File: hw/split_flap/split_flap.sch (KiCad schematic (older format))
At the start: 22 parts, among them J1 Conn_01x02, J19 POWER, J2 Conn_01x02, J3 Conn_01x02, J4 Conn_01x02, J5 Conn_01x02, J6 Conn_01x02, J7 Conn_01x02, J8 Conn_01x02, SW1 SW_RESET, U1 PCF8574, U2 NodeMCU_1.0_(ESP-12E)

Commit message: hw: Supercharge PCB !
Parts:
- removed SW1: SW_RESET, Connector_PinHeader_2.54mm:PinHeader_1x02_P2.54mm_Vertical, symbol Switch:SW_Push
- added J17: Conn_01x05, Connector_JST:JST_XH_B5B-XH-A_1x05_P2.50mm_Vertical, symbol Connector_Generic:Conn_01x05
- added J23, J24, J25, J26: Conn_01x02, Connector_JST:JST_XH_B2B-XH-A_1x02_P2.50mm_Vertical, symbol Connector_Generic:Conn_01x02
- added R11, R12, R13, R14: R, Resistor_THT:R_Axial_DIN0207_L6.3mm_D2.5mm_P10.16mm_Horizontal, symbol Device:R
- added U15: PCF8574, Package_SO:SOIC-16W_7.5x10.3mm_P1.27mm, symbol Interface_Expansion:PCF8574
- U2: footprint ESP:NodeMCU1.0(12-E) -> ESP:ESP12F-Devkit-V3
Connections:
- wire segments 121 -> 175
- no-connect marks 22 -> 30
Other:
- moved on the sheet: J1, J19, J2, J3, J4, J5, J6, J7, J8, R1, R10, R2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

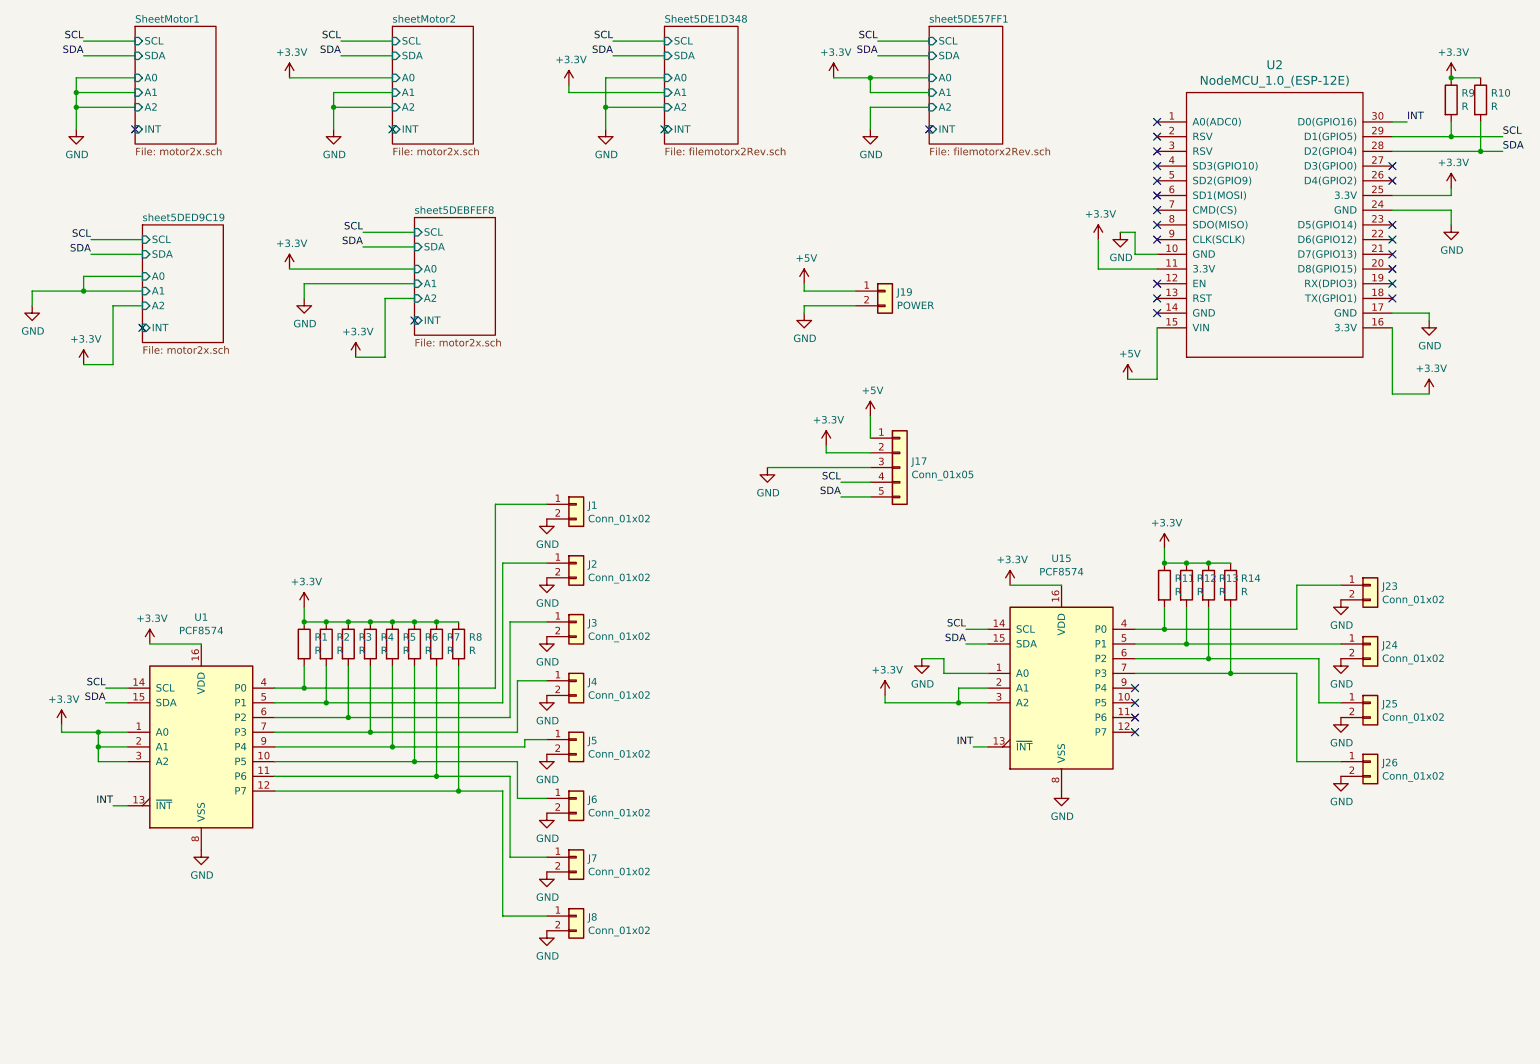
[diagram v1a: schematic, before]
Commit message: Reroute full PCB
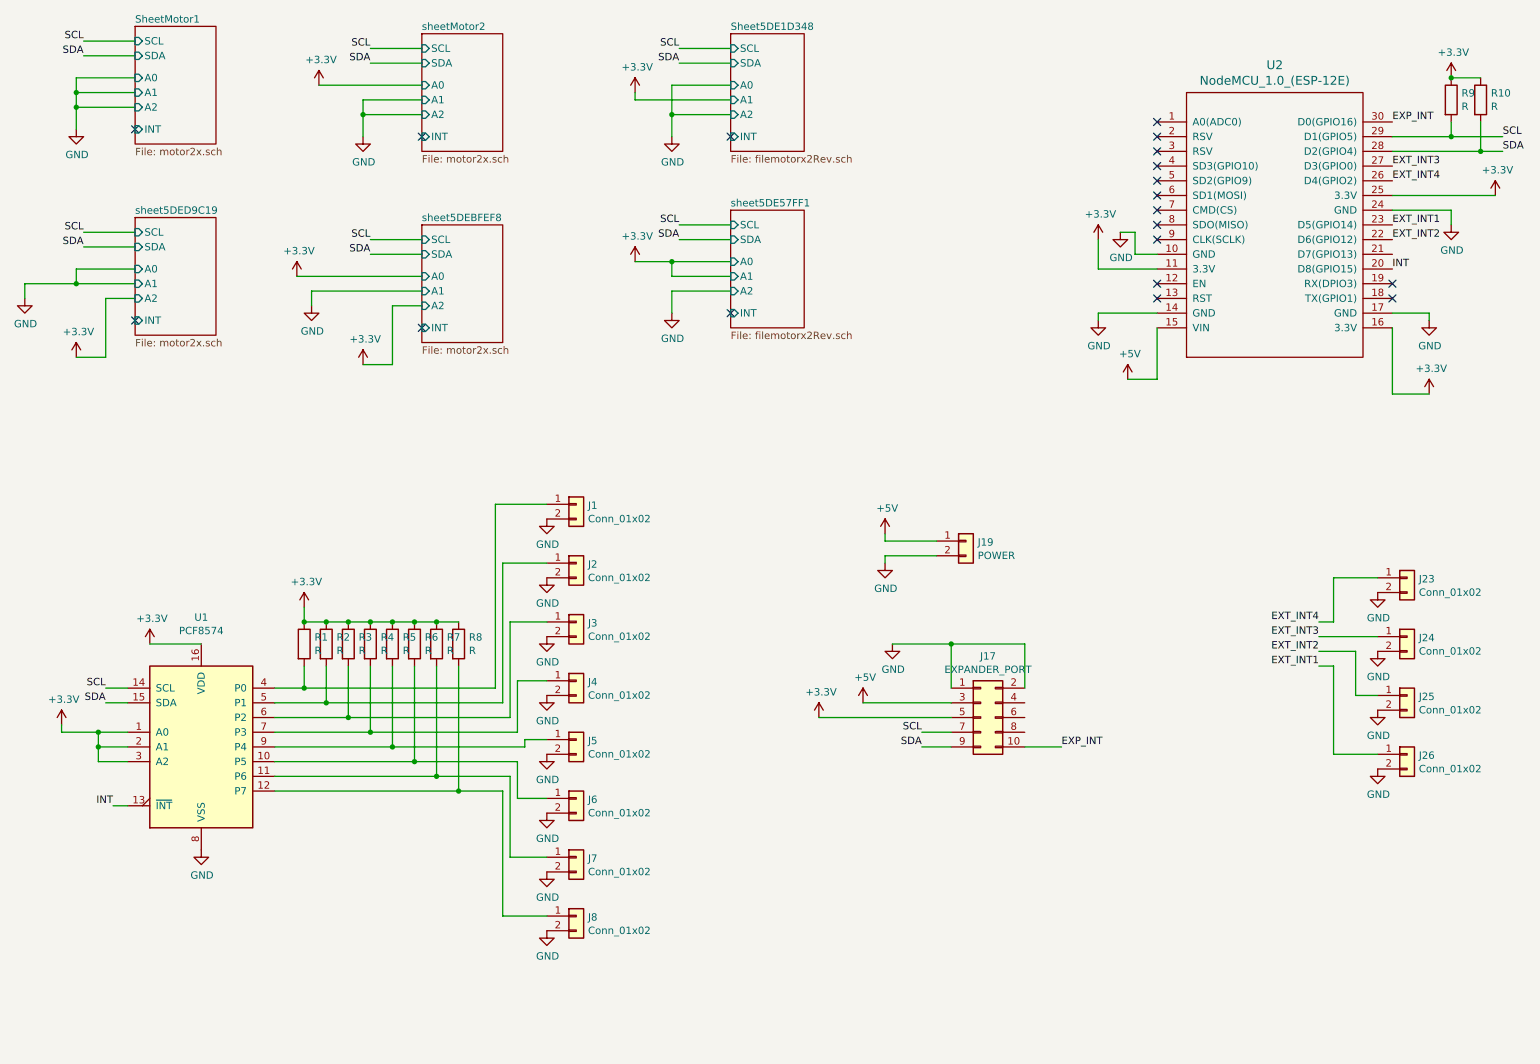
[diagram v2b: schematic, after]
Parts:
- removed J17: Conn_01x05, Connector_JST:JST_XH_B5B-XH-A_1x05_P2.50mm_Vertical, symbol Connector_Generic:Conn_01x05
- removed R11, R12, R13, R14: R, Resistor_THT:R_Axial_DIN0207_L6.3mm_D2.5mm_P10.16mm_Horizontal, symbol Device:R
- removed U15: PCF8574, Package_SO:SOIC-16W_7.5x10.3mm_P1.27mm, symbol Interface_Expansion:PCF8574
- added J17: EXPANDER_PORT, Connector_PinHeader_2.54mm:PinHeader_2x05_P2.54mm_Vertical, symbol Connector_Generic:Conn_02x05_Odd_Even
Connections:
- net +3V3: now also J17.5 (Pin_5)
- net +5V: now also J17.3 (Pin_3)
- net GND: now also U2.14 (GND), J17.1 (Pin_1), J17.2 (Pin_2)
- net INT: now also U2.20 (D8(GPIO15)); no longer U2.30 (D0(GPIO16))
- net SCL: now also J17.7 (Pin_7)
- net SDA: now also J17.9 (Pin_9)
- net EXT_INT2: now reaches U2.22 (D6(GPIO12))
- net EXT_INT2: now also J25.1 (Pin_1)
- net EXT_INT1: now reaches U2.23 (D5(GPIO14))
- net EXT_INT1: now also J26.1 (Pin_1)
- net EXT_INT4: now reaches U2.26 (D4(GPIO2))
- net EXT_INT4: now also J23.1 (Pin_1)
- net EXT_INT3: now reaches U2.27 (D3(GPIO0))
- net EXT_INT3: now also J24.1 (Pin_1)
- new net EXP_INT: J17.10 (Pin_10), U2.30 (D0(GPIO16))
- no-connect marks 30 -> 19
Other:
- moved on the sheet: J19, J23, J24, J25, J26

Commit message: hw: Route pcb completely
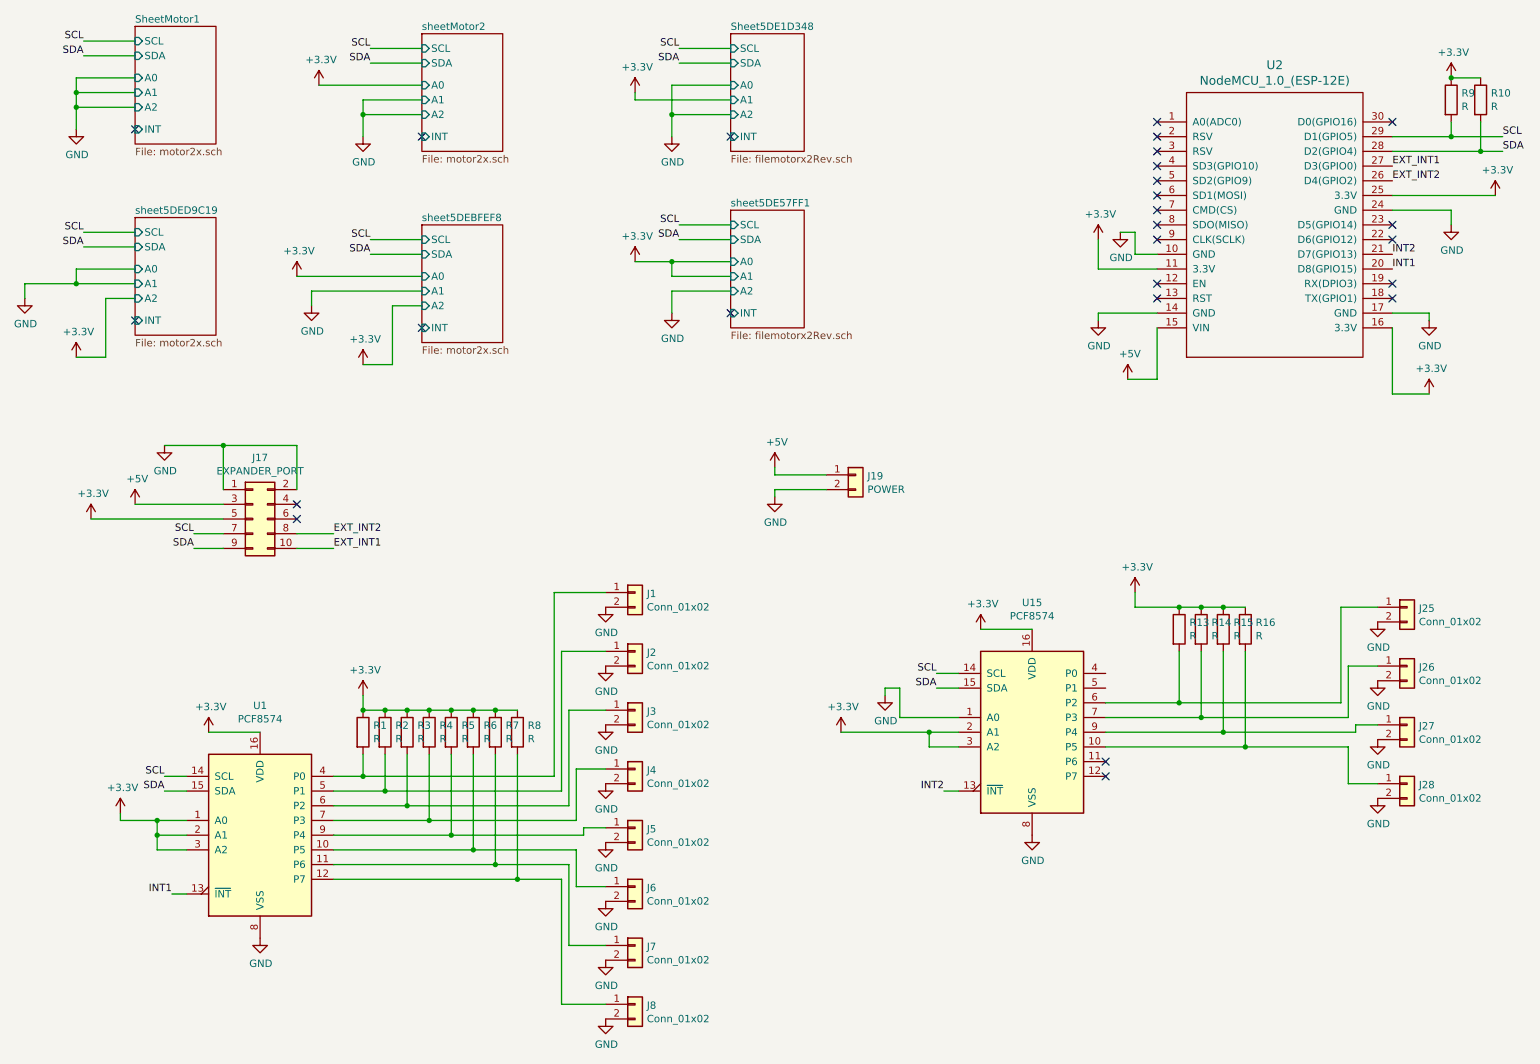
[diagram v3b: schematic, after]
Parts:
- removed J23, J24: Conn_01x02, Connector_JST:JST_XH_B2B-XH-A_1x02_P2.50mm_Vertical, symbol Connector_Generic:Conn_01x02
- added J27, J28: Conn_01x02, Connector_JST:JST_XH_B2B-XH-A_1x02_P2.50mm_Vertical, symbol Connector_Generic:Conn_01x02
- added R13, R14, R15, R16: R, Resistor_SMD:R_0805_2012Metric_Pad1.15x1.40mm_HandSolder, symbol Device:R
- added U15: PCF8574, Package_SO:SOIC-16W_7.5x10.3mm_P1.27mm, symbol Interface_Expansion:PCF8574
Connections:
- net EXT_INT3 is gone; now on net EXT_INT1: U2.27 (D3(GPIO0))
- net EXT_INT4 is gone; now on net EXT_INT2: U2.26 (D4(GPIO2))
- net +3V3: now also R13.1, R14.1, R15.1, R16.1, U15.16 (VDD), U15.2 (A1), U15.3 (A2)
- net EXT_INT1: now also J17.10 (Pin_10); no longer J26.1 (Pin_1), U2.23 (D5(GPIO14))
- net EXT_INT2: now also J17.8 (Pin_8); no longer J25.1 (Pin_1), U2.22 (D6(GPIO12))
- net GND: now also J27.2 (Pin_2), J28.2 (Pin_2), U15.1 (A0), U15.8 (VSS)
- net SCL: now also U15.14 (SCL)
- net SDA: now also U15.15 (SDA)
- net INT2: now reaches U2.21 (D7(GPIO13))
- net INT2: now also U15.13 (~INT~)
- net EXP_INT: no longer names the net of U2.30 (D0(GPIO16))
- net EXP_INT: no longer J17.10 (Pin_10)
- net INT renamed INT1
- new net: J28.1 (Pin_1), R16.2, U15.10 (P5)
- new net: J25.1 (Pin_1), R13.2, U15.6 (P2)
- new net: J26.1 (Pin_1), R14.2, U15.7 (P3)
- new net: J27.1 (Pin_1), R15.2, U15.9 (P4)
- no-connect marks 19 -> 26
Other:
- moved on the sheet: J1, J17, J19, J2, J25, J26, J3, J4, J5, J6, J7, J8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

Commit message: Update schematic with 74HC595
Remove PCF for output and use shift register
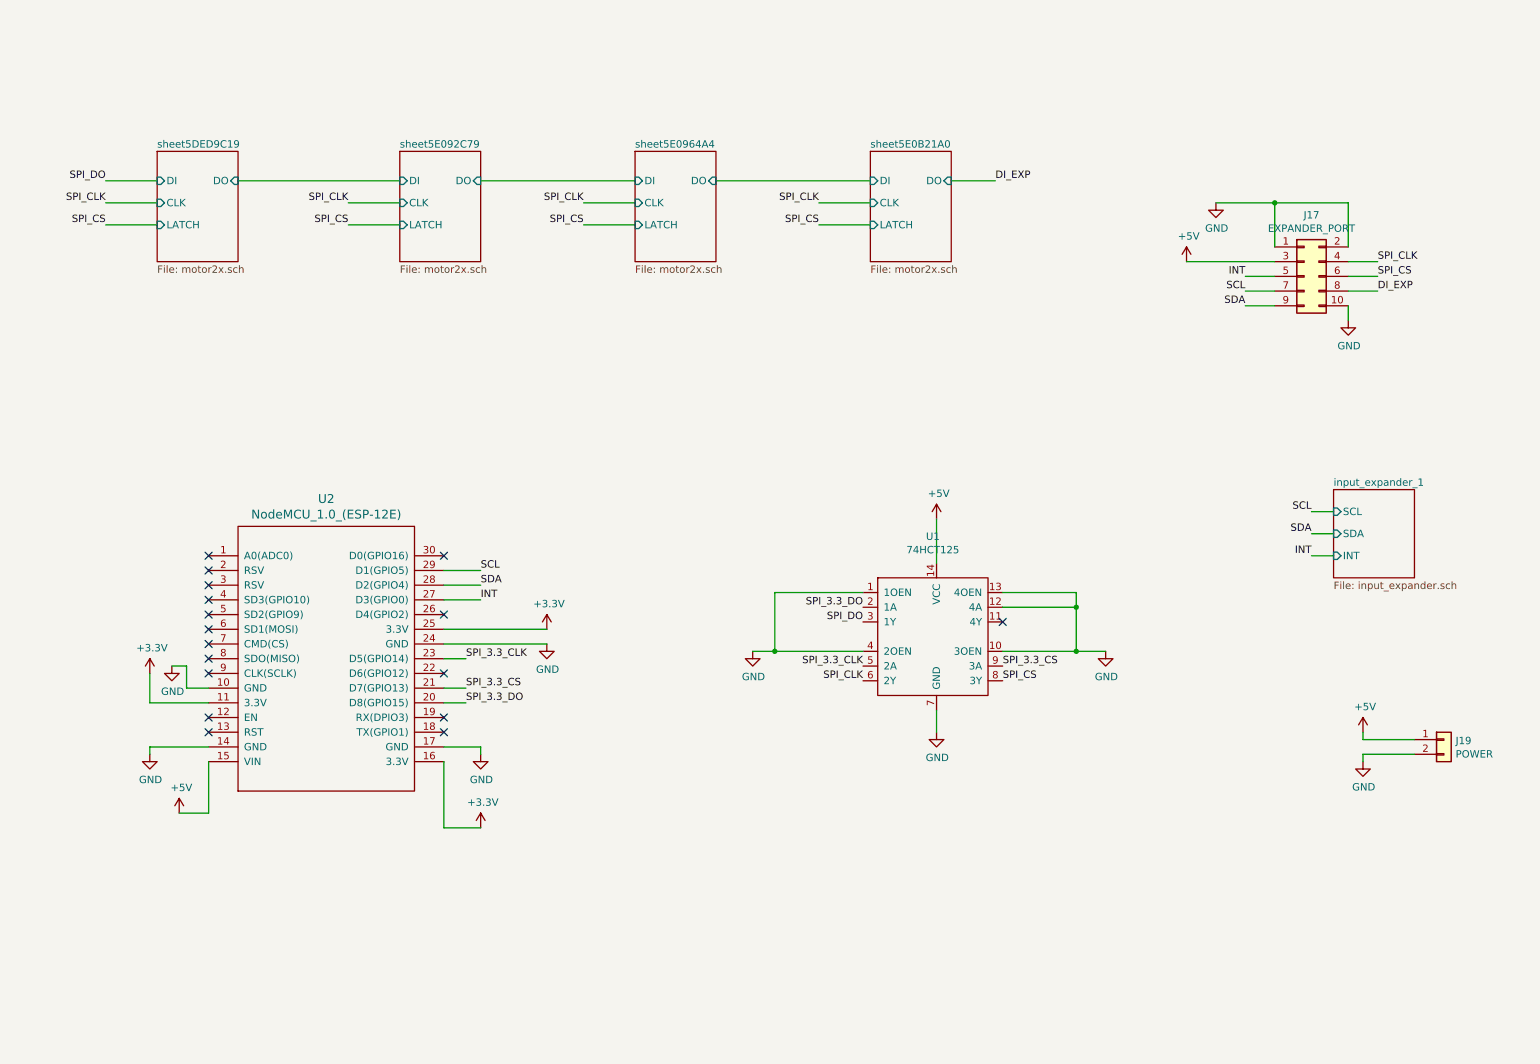
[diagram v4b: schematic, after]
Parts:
- removed J1, J2, J25, J26, J27, J28, J3, J4, J5, J6, J7, J8: Conn_01x02, Connector_JST:JST_XH_B2B-XH-A_1x02_P2.50mm_Vertical, symbol Connector_Generic:Conn_01x02
- removed R1, R10, R2, R3, R4, R5, R6, R7, R8, R9: R, Resistor_THT:R_Axial_DIN0207_L6.3mm_D2.5mm_P10.16mm_Horizontal, symbol Device:R
- removed R13, R14, R15, R16: R, Resistor_SMD:R_0805_2012Metric_Pad1.15x1.40mm_HandSolder, symbol Device:R
- removed U1, U15: PCF8574, Package_SO:SOIC-16W_7.5x10.3mm_P1.27mm, symbol Interface_Expansion:PCF8574
- added U1: 74HCT125, symbol 74HCT125:74HCT125
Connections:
- net +3V3: no longer J17.5 (Pin_5)
- net +5V: now also U1.14 (VCC)
- net GND: now also J17.10 (Pin_10), U1.1 (1OEN), U1.10 (3OEN), U1.12 (4A), U1.13 (4OEN), U1.4 (2OEN), U1.7 (GND)
- net SPI_3.3_CLK: now reaches U2.23 (D5(GPIO14))
- net SPI_3.3_CLK: now also U1.5 (2A)
- net SPI_CLK: now reaches J17.4 (Pin_4)
- net SPI_CLK: now also U1.6 (2Y)
- net SPI_CS: now reaches J17.6 (Pin_6)
- net SPI_CS: now also U1.8 (3Y)
- net EXT_INT1 renamed INT
- net INT: now also J17.5 (Pin_5); no longer J17.10 (Pin_10)
- net EXT_INT2: no longer names the net of U2.26 (D4(GPIO2))
- net EXT_INT2: no longer J17.8 (Pin_8)
- net INT1 renamed SPI_3.3_DO
- net SPI_3.3_DO: now also U1.2 (1A)
- net INT2 renamed SPI_3.3_CS
- net SPI_3.3_CS: now also U1.9 (3A)
- new net DI_EXP: J17.8 (Pin_8)
- new net SPI_DO: U1.3 (1Y)
- no-connect marks 26 -> 17
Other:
- moved on the sheet: J17, J19, U2
